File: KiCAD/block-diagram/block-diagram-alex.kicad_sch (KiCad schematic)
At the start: 35 parts, among them J1 Conn_01x08, J2 Conn_01x08, J3 Conn_01x10, Q3 NMOS, Q4 NMOS, U1 74HC02, U3 74HC11, U6 LMC555xM

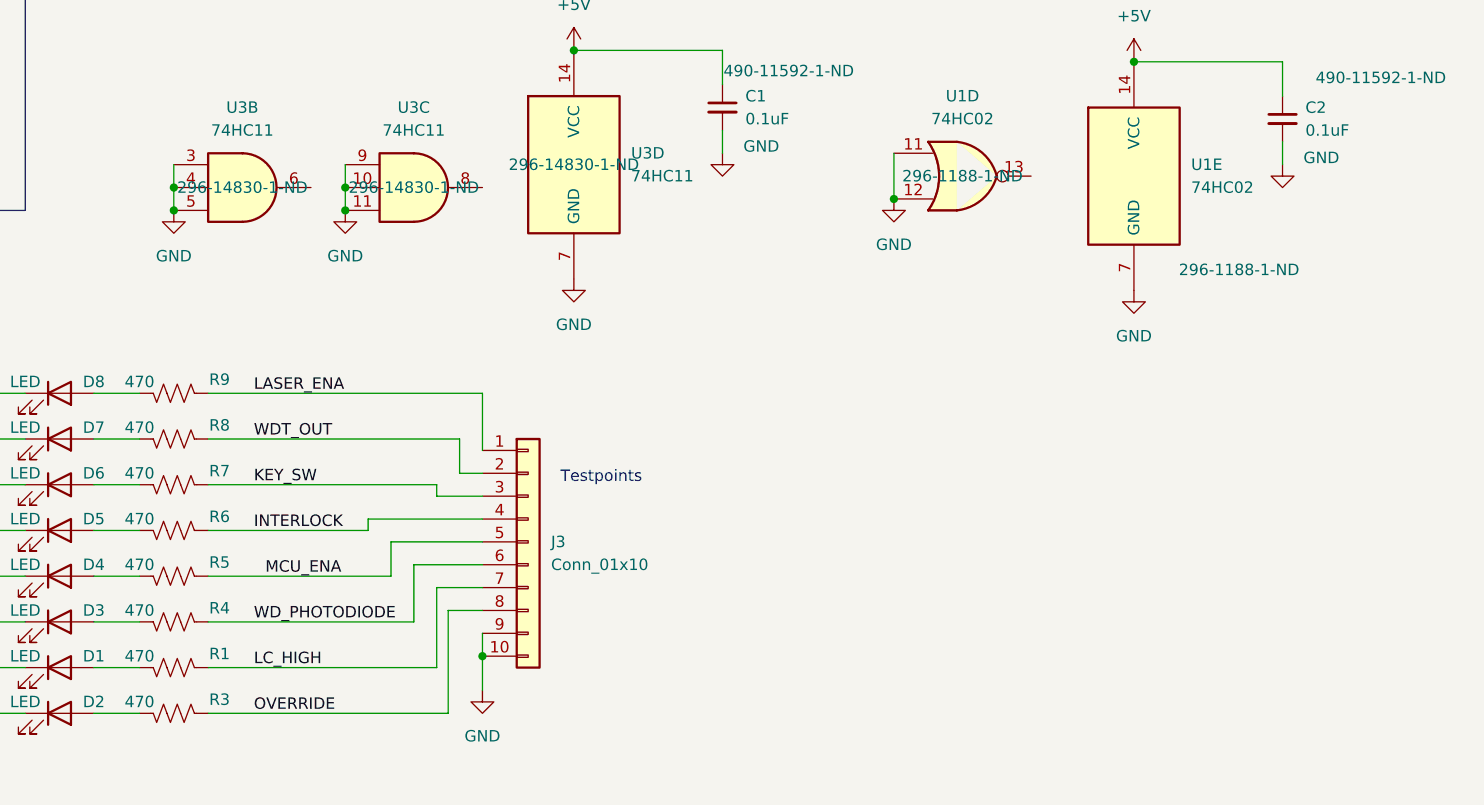
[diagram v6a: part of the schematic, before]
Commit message: Resistor part numbers for LED resistors
Added part and manufacturer numbers for the resistors connected to the LED
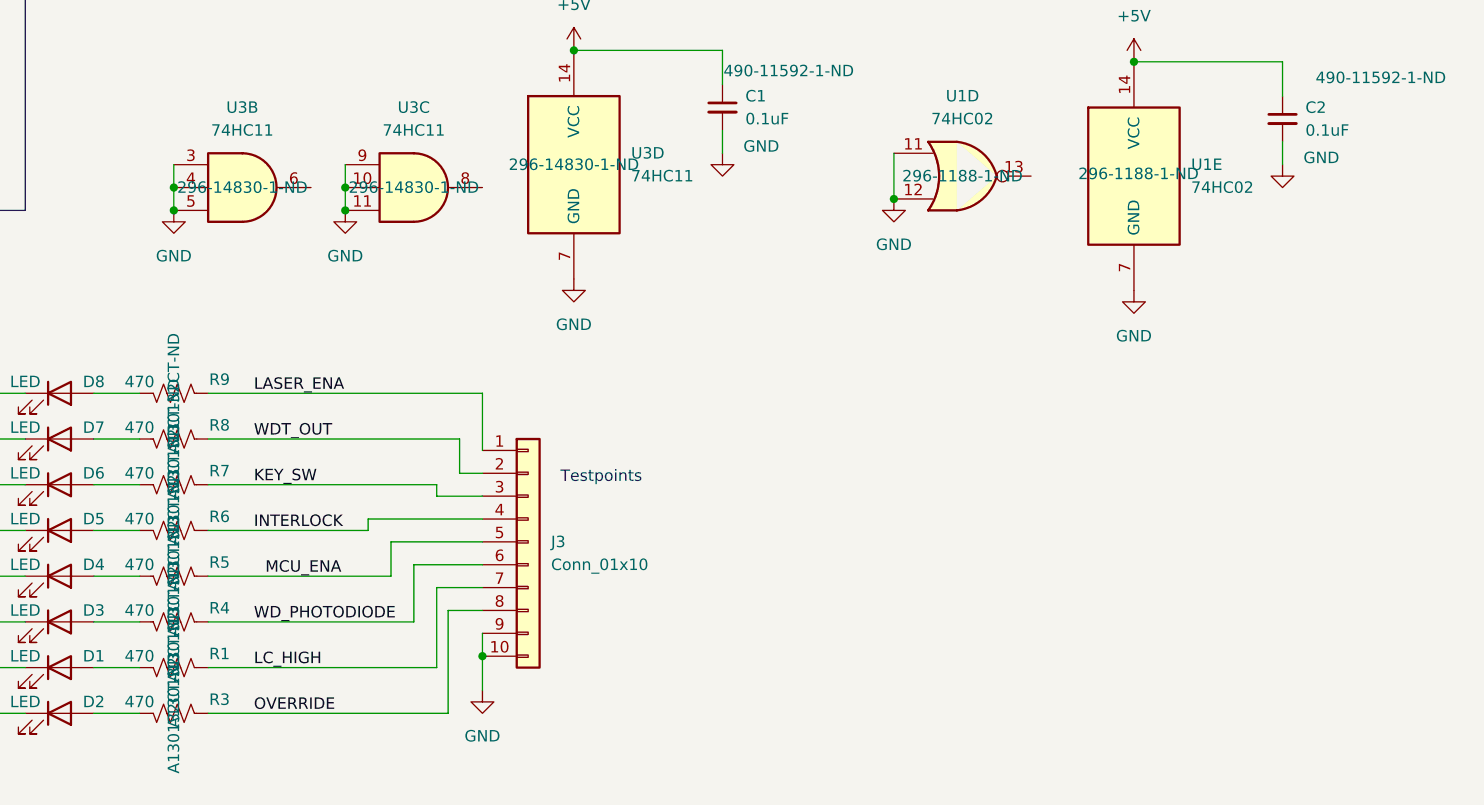
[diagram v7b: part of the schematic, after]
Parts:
- R1, R3, R4, R5, R6, R7, R8, R9: CatNo (none) -> A130132CT-ND; MfgNo (none) -> CRGCQ0805J470R
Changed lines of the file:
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@@
 			)
 		)
+		(property "CatNo" "A130132CT-ND"
+			(at 105.41 179.07 0)
+			(effects
+				(font
+					(size 1.27 1.27)
+				)
+			)
+		)
+		(property "MfgNo" "CRGCQ0805J470R"
+			(at 105.41 179.07 0)
+			(effects
+				(font
+					(size 1.27 1.27)
+				)
+				(hide yes)
+			)
+		)
 		(pin "1"
 		)
@@
 			)
 		)
+		(property "CatNo" "A130132CT-ND"
+			(at 105.41 184.15 0)
+			(effects
+				(font
+					(size 1.27 1.27)
+				)
+			)
+		)
+		(property "MfgNo" "CRGCQ0805J470R"
+			(at 105.41 184.15 0)
+			(effects
+				(font
+					(size 1.27 1.27)
+				)
+				(hide yes)
+			)
+		)
 		(pin "1"
 		)
@@
 		)
 		(property "CatNo" "296-1188-1-ND"
-			(at 223.774 139.954 0)
+			(at 212.598 129.286 0)
 			(effects
 				(font
@@
 			)
 		)
+		(property "CatNo" "A130132CT-ND"
+			(at 105.41 153.67 0)
+			(effects
+				(font
+					(size 1.27 1.27)
+				)
+			)
+		)
+		(property "MfgNo" "CRGCQ0805J470R"
+			(at 105.41 153.67 0)
+			(effects
+				(font
+					(size 1.27 1.27)
+				)
+				(hide yes)
+			)
+		)
 		(pin "1"
 		)
@@
 			)
 		)
+		(property "CatNo" "A130132CT-ND"
+			(at 105.41 173.99 0)
+			(effects
+				(font
+					(size 1.27 1.27)
+				)
+			)
+		)
+		(property "MfgNo" "CRGCQ0805J470R"
+			(at 105.41 173.99 0)
+			(effects
+				(font
+					(size 1.27 1.27)
+				)
+				(hide yes)
+			)
+		)
 		(pin "1"
 		)
@@
 			)
 		)
+		(property "CatNo" "A130132CT-ND"
+			(at 105.41 189.23 0)
+			(effects
+				(font
+					(size 1.27 1.27)
+				)
+			)
+		)
+		(property "MfgNo" "CRGCQ0805J470R"
+			(at 105.41 189.23 0)
+			(effects
+				(font
+					(size 1.27 1.27)
+				)
+				(hide yes)
+			)
+		)
 		(pin "1"
 		)
@@
 			)
 		)
+		(property "CatNo" "A130132CT-ND"
+			(at 105.41 163.83 0)
+			(effects
+				(font
+					(size 1.27 1.27)
+				)
+			)
+		)
+		(property "MfgNo" "CRGCQ0805J470R"
+			(at 105.41 163.83 0)
+			(effects
+				(font
+					(size 1.27 1.27)
+				)
+				(hide yes)
+			)
+		)
 		(pin "1"
 		)
@@
 			)
 		)
+		(property "CatNo" "A130132CT-ND"
+			(at 105.41 158.75 0)
+			(effects
+				(font
+					(size 1.27 1.27)
+				)
+			)
+		)
+		(property "MfgNo" "CRGCQ0805J470R"
+			(at 105.41 158.75 0)
+			(effects
+				(font
+					(size 1.27 1.27)
+				)
+				(hide yes)
+			)
+		)
 		(pin "1"
 		)
@@
 			(at 105.41 168.91 0)
 			(effects
+				(font
+					(size 1.27 1.27)
+				)
+				(hide yes)
+			)
+		)
+		(property "CatNo" "A130132CT-ND"
+			(at 105.41 168.91 0)
+			(effects
+				(font
+					(size 1.27 1.27)
+				)
+			)
+		)
+		(property "MfgNo" "CRGCQ0805J470R"
+			(at 105.41 168.91 0)
+			(effects

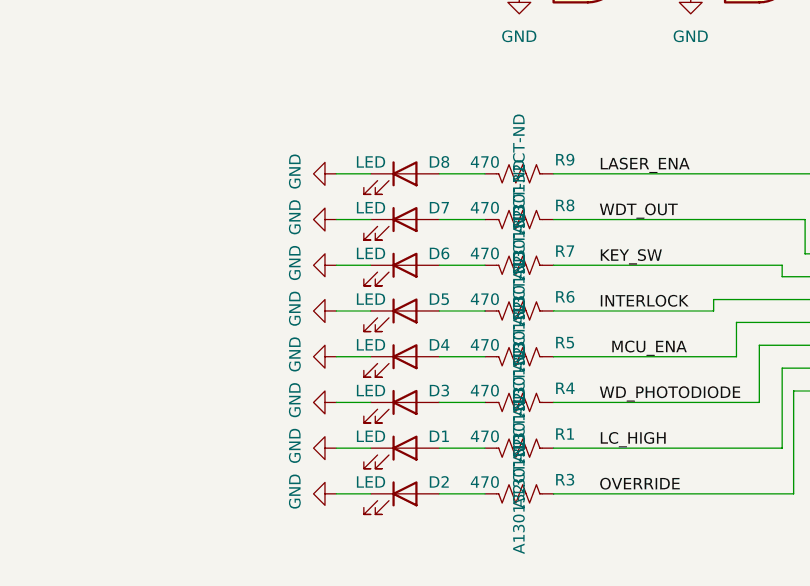
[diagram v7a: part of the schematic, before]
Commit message: LED part number
Added part and manufacturer numbers for the LEDs
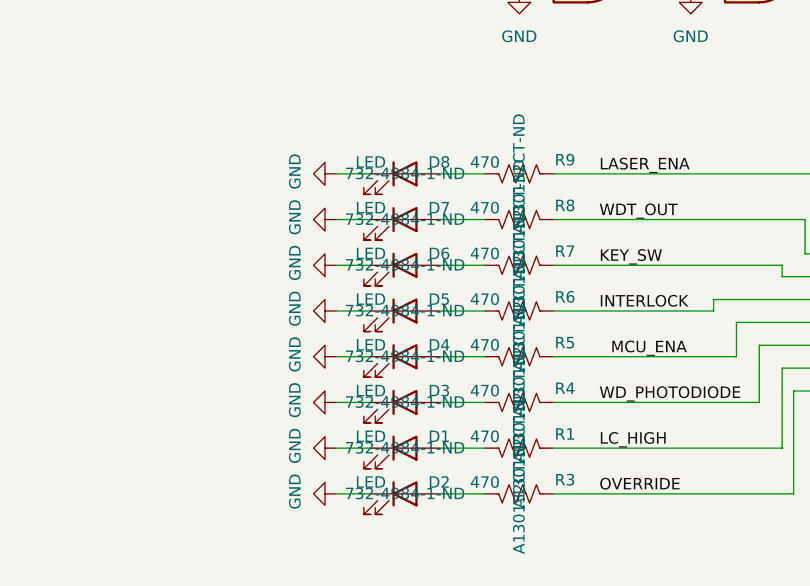
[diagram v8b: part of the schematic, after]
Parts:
- D1, D2, D3, D4, D5, D6, D7, D8: CatNo (none) -> 732-4984-1-ND; MfgNo (none) -> 150080RS75000
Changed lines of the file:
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@@
 			)
 		)
+		(property "CatNo" "732-4984-1-ND"
+			(at 92.71 158.75 0)
+			(effects
+				(font
+					(size 1.27 1.27)
+				)
+			)
+		)
+		(property "MfgNo" "150080RS75000"
+			(at 92.71 158.75 0)
+			(effects
+				(font
+					(size 1.27 1.27)
+				)
+				(hide yes)
+			)
+		)
 		(pin "1"
 		)
@@
 			)
 		)
+		(property "CatNo" "732-4984-1-ND"
+			(at 92.71 163.83 0)
+			(effects
+				(font
+					(size 1.27 1.27)
+				)
+			)
+		)
+		(property "MfgNo" "150080RS75000"
+			(at 92.71 163.83 0)
+			(effects
+				(font
+					(size 1.27 1.27)
+				)
+				(hide yes)
+			)
+		)
 		(pin "1"
 		)
@@
 			)
 		)
+		(property "CatNo" "732-4984-1-ND"
+			(at 92.71 184.15 0)
+			(effects
+				(font
+					(size 1.27 1.27)
+				)
+			)
+		)
+		(property "MfgNo" "150080RS75000"
+			(at 92.71 184.15 0)
+			(effects
+				(font
+					(size 1.27 1.27)
+				)
+				(hide yes)
+			)
+		)
 		(pin "1"
 		)
@@
 			)
 		)
+		(property "CatNo" "732-4984-1-ND"
+			(at 92.71 173.99 0)
+			(effects
+				(font
+					(size 1.27 1.27)
+				)
+			)
+		)
+		(property "MfgNo" "150080RS75000"
+			(at 92.71 173.99 0)
+			(effects
+				(font
+					(size 1.27 1.27)
+				)
+				(hide yes)
+			)
+		)
 		(pin "1"
 		)
@@
 			)
 		)
+		(property "CatNo" "732-4984-1-ND"
+			(at 92.71 179.07 0)
+			(effects
+				(font
+					(size 1.27 1.27)
+				)
+			)
+		)
+		(property "MfgNo" "150080RS75000"
+			(at 92.71 179.07 0)
+			(effects
+				(font
+					(size 1.27 1.27)
+				)
+				(hide yes)
+			)
+		)
 		(pin "1"
 		)
@@
 			)
 		)
+		(property "CatNo" "732-4984-1-ND"
+			(at 92.71 168.91 0)
+			(effects
+				(font
+					(size 1.27 1.27)
+				)
+			)
+		)
+		(property "MfgNo" "150080RS75000"
+			(at 92.71 168.91 0)
+			(effects
+				(font
+					(size 1.27 1.27)
+				)
+				(hide yes)
+			)
+		)
 		(pin "1"
 		)
@@
 			)
 		)
+		(property "CatNo" "732-4984-1-ND"
+			(at 92.71 153.67 0)
+			(effects
+				(font
+					(size 1.27 1.27)
+				)
+			)
+		)
+		(property "MfgNo" "150080RS75000"
+			(at 92.71 153.67 0)
+			(effects
+				(font
+					(size 1.27 1.27)
+				)
+				(hide yes)
+			)
+		)
 		(pin "1"
 		)
@@
 			(at 92.71 189.23 0)
 			(effects
+				(font
+					(size 1.27 1.27)
+				)
+				(hide yes)
+			)
+		)
+		(property "CatNo" "732-4984-1-ND"
+			(at 92.71 189.23 0)
+			(effects
+				(font
+					(size 1.27 1.27)
+				)
+			)
+		)
+		(property "MfgNo" "150080RS75000"
+			(at 92.71 189.23 0)
+			(effects
